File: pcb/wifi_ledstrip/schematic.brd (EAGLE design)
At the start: 160 x 100 mm, 1 part, among them IC1 STM32F10XCXT6

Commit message: main parts added
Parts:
- added HEARTBEAT, LED7, LED8, L_12V, L_3V3, L_5V, L_RX, L_TX: (no value), led:SML1206
- added LED_STRIP_12V, LED_STRIP_GND, LED_STRIP_SIGNAL: (no value), SparkFun-Connectors:SCREWTERMINAL-3.5MM-3
- added POWER: (no value), SparkFun-Connectors:SCREWTERMINAL-5MM-2
- added PROGRAMMER: (no value), SparkFun-Connectors:MOLEX-1X3
- added SW_3, SW_4, SW_RESET, WIFI_RECONNECT: TACTILE_SWITCH_SIDETACTILE_SWITCH_SIDE, mylibrary:TACTILE_SWITCH_SIDE
- added U$1, U$2, U$3: SN74LV1T34, mylibrary:SOT-23-5
- added WIFI_MODUL: ESP01, esp8266modules:ESP01
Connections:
- new net GND: U$1.3, U$2.3, U$3.3
- new net LED_STRIP_SIGNAL_1: U$3.2
- new net LED_STRIP_SIGNAL_2: U$1.2
- new net LED_STRIP_SIGNAL_3: U$2.2
- new net N$1: LED_STRIP_SIGNAL.3, U$2.4
- new net N$2: LED_STRIP_SIGNAL.2, U$1.4
- new net N$3: LED_STRIP_SIGNAL.1, U$3.4
- new net VCC: U$1.5, U$2.5, U$3.5

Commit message: mikrocontroller capacitances, boot pins, reset button added
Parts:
- added C1, C3, C7: (no value), rcl:C1206
- added C10: 1u, rcl:C1206
- added C2: 0.1u, rcl:C1206
- added C4, C5, C6: 100n, rcl:C1206
- added C9: 10n, rcl:C1206
- added C_VDD3: 4.7u, rcl:C1206
- added Q1: 8MHz, special:QS
- added R1, R2, R3, R4, R5, R7, R8, R9: (no value), rcl:R1206
- added R10: 100k, rcl:R1206
- added R11, R6: 10k, rcl:R1206
- HEARTBEAT, LED7, LED8, L_12V, L_3V3, L_5V, L_RX, L_TX: value (none) -> GREEN; device led:SML1206 -> SparkFun-LED:LED-1206
- moved LED_STRIP_SIGNAL 117.7 mm to (-35.6, -119.4)
- moved L_12V 113.5 mm to (3.81, 2.54)
- moved U$3 26.9 mm to (-40.6, -124.5)
- moved U$1 21.7 mm to (-36.8, -129.5), turned to 90 degrees
- moved U$2 18.0 mm to (-31.8, -133.3)
- moved LED_STRIP_12V 4.02 mm to (-8.89, -10.2)
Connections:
- removed net VBAT: IC1.1
- removed net VDDA: IC1.9
- removed net VDD_1: IC1.24
- removed net VDD_2: IC1.36
- removed net VDD_3: IC1.48
- removed net VSSA: IC1.8
- removed net VSS_1: IC1.23
- removed net VSS_2: IC1.35
- removed net VSS_3: IC1.47
- new net BTN_3: SW_3.P$5
- new net BTN_4: SW_4.P$5
- new net BTN_WIFI_RECONNECT: WIFI_RECONNECT.P$5
- new net HEARTBEAT: R7.1
- new net LED7: R8.1
- new net LED8: R9.1
- new net N$10: HEARTBEAT.A, R7.2
- new net N$11: LED7.A, R8.2
- new net N$12: LED8.A, R9.2
- new net N$13: C2.1, IC1.7, SW_RESET.P$3
- new net N$14: C3.1, IC1.5, Q1.2
- new net N$15: C7.1, IC1.6, Q1.1
- new net N$16: IC1.44, R11.2
- new net N$17: PROGRAMMER.2
- new net N$18: PROGRAMMER.3, R10.1
- new net N$4: L_12V.A, R1.1
- new net N$5: L_5V.A, R2.1
- new net N$6: L_3V3.A, R3.1
- new net N$7: L_RX.A, R4.1
- new net N$8: R6.1, WIFI_MODUL.CH_PD
- new net N$9: L_TX.A, R5.1
- new net UART_RX: L_RX.C, WIFI_MODUL.TX
- new net UART_TX: L_TX.C, WIFI_MODUL.RX
- net GND: now also C1.2, C10.2, C2.2, C3.2, C4.2, C5.2, C6.2, C7.2, C9.2, C_VDD3.2, HEARTBEAT.C, IC1.23, IC1.35, IC1.47, IC1.8, LED7.C, LED8.C, LED_STRIP_GND.1, LED_STRIP_GND.2, LED_STRIP_GND.3, L_12V.C, L_3V3.C, L_5V.C, POWER.1, PROGRAMMER.1, R11.1, SW_3.P$3, SW_4.P$3, SW_RESET.P$5, WIFI_MODUL.GND, WIFI_RECONNECT.P$3
- net VCC: now also C1.1, C10.1, C4.1, C5.1, C6.1, C9.1, C_VDD3.1, IC1.1, IC1.24, IC1.36, IC1.48, IC1.9, LED_STRIP_12V.1, LED_STRIP_12V.2, LED_STRIP_12V.3, POWER.2, R1.2, R10.2, R2.2, R3.2, R4.2, R5.2, R6.2, WIFI_MODUL.VCC
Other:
- board size 160 x 100 mm -> 99 x 100 mm

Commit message: parts added, psu symbols fixed
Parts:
- added C11, C15: 8.2n, rcl:C1206
- added C12, C16: 100n, rcl:C1206
- added C13, C14, C17, C8: 22u, rcl:C1206
- added R12, R15: 100k, rcl:R1206
- added R13: 33.2, rcl:R1206
- added R14, R17, R18, R19: 10k, rcl:R1206
- added R16: 56.2k, rcl:R1206
- added SRN4026-4R7M: 4.7u, mylibrary:SRN4026-4R7M
- added TYS60203R3N-10: 3.3u, mylibrary:TYS60203R3N-10
- added U$4, U$5: TPS562219A, mylibrary:SOT23-8L
- C3, C7: value (none) -> 20p
- moved R11 306.7 mm to (45.7, 14.0)
- moved C10 306.7 mm to (45.7, 45.7)
- moved C3 306.7 mm to (45.7, 24.1)
- moved C7 306.7 mm to (45.7, 19.1)
- moved C9 306.7 mm to (45.7, 50.8)
- moved Q1 306.7 mm to (49.5, 31.8)
- moved R10 306.7 mm to (45.7, 7.62)
- moved C1 265.2 mm to (36.8, 66.0)
- moved C2 265.2 mm to (36.8, 45.7)
- moved C4 265.2 mm to (36.8, 35.6)
- moved C5 265.2 mm to (36.8, 30.5)
- moved C6 265.2 mm to (36.8, 25.4)
- moved C_VDD3 265.2 mm to (36.8, 40.6)
- moved R1 265.2 mm to (36.8, 96.5)
- moved R2 265.2 mm to (36.8, 91.4)
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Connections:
- removed net LED7: R8.1
- removed net LED8: R9.1
- removed net VCC: C1.1, C10.1, C4.1, C5.1, C6.1, C9.1, C_VDD3.1, IC1.1, IC1.24, IC1.36, IC1.48, IC1.9, LED_STRIP_12V.1, LED_STRIP_12V.2, LED_STRIP_12V.3, POWER.2, R1.2, R10.2, R2.2, R3.2, R4.2, R5.2, R6.2, U$1.5, U$2.5, U$3.5, WIFI_MODUL.VCC
- new net +12V: C14.1, C8.1, LED_STRIP_12V.1, LED_STRIP_12V.2, LED_STRIP_12V.3, POWER.2, R1.2, R18.1, R19.1, U$4.3, U$5.3
- new net +3V3: C1.1, C10.1, C13.1, C4.1, C5.1, C6.1, C9.1, C_VDD3.1, IC1.1, IC1.24, IC1.36, IC1.48, IC1.9, R10.2, R12.2, R13.2, R3.2, R4.2, R5.2, R6.2, TYS60203R3N-10.P$2, WIFI_MODUL.VCC
- new net +5V: C17.1, R15.2, R16.2, R2.2, SRN4026-4R7M.P$3, U$1.5, U$2.5, U$3.5
- new net LED_7: IC1.3, R8.1
- new net LED_8: IC1.4, R9.1
- new net N$19: IC1.40
- new net N$20: IC1.41
- new net N$21: IC1.42
- new net N$22: IC1.43
- new net N$23: IC1.45
- new net N$24: IC1.46
- new net N$25: C11.1, U$4.5
- new net N$26: C12.1, TYS60203R3N-10.P$1, U$4.2
- new net N$27: IC1.28
- new net N$28: R12.1, U$4.4
- new net N$29: U$4.6
- new net N$30: C15.1, U$5.5
- new net N$31: C16.2, U$5.8
- new net N$32: R13.1, R14.2
- new net N$33: C16.1, SRN4026-4R7M.P$2, U$5.2
- new net N$34: R15.1, U$5.4
- new net N$35: U$5.6
- new net N$36: R16.1, R17.2
- new net N$37: R18.2, U$4.7
- new net N$38: R19.2, U$5.7
- new net SWCLK: IC1.37, PROGRAMMER.2
- new net SWDIO: IC1.34, PROGRAMMER.3, R10.1
- net BTN_3: now also IC1.26
- net BTN_4: now also IC1.27
- net BTN_WIFI_RECONNECT: now also IC1.25
- net GND: now also C11.2, C13.2, C14.2, C15.2, C17.2, C8.2, R14.1, R17.1, U$4.1, U$5.1
- net HEARTBEAT: now also IC1.2
- net LED_STRIP_SIGNAL_1: now also IC1.17
- net LED_STRIP_SIGNAL_2: now also IC1.18
- net LED_STRIP_SIGNAL_3: now also IC1.19
- net N$17: now also C12.2, U$4.8; no longer PROGRAMMER.2
- net N$18: now also IC1.39; no longer PROGRAMMER.3, R10.1
- net UART_RX: now also IC1.31
- net UART_TX: now also IC1.30

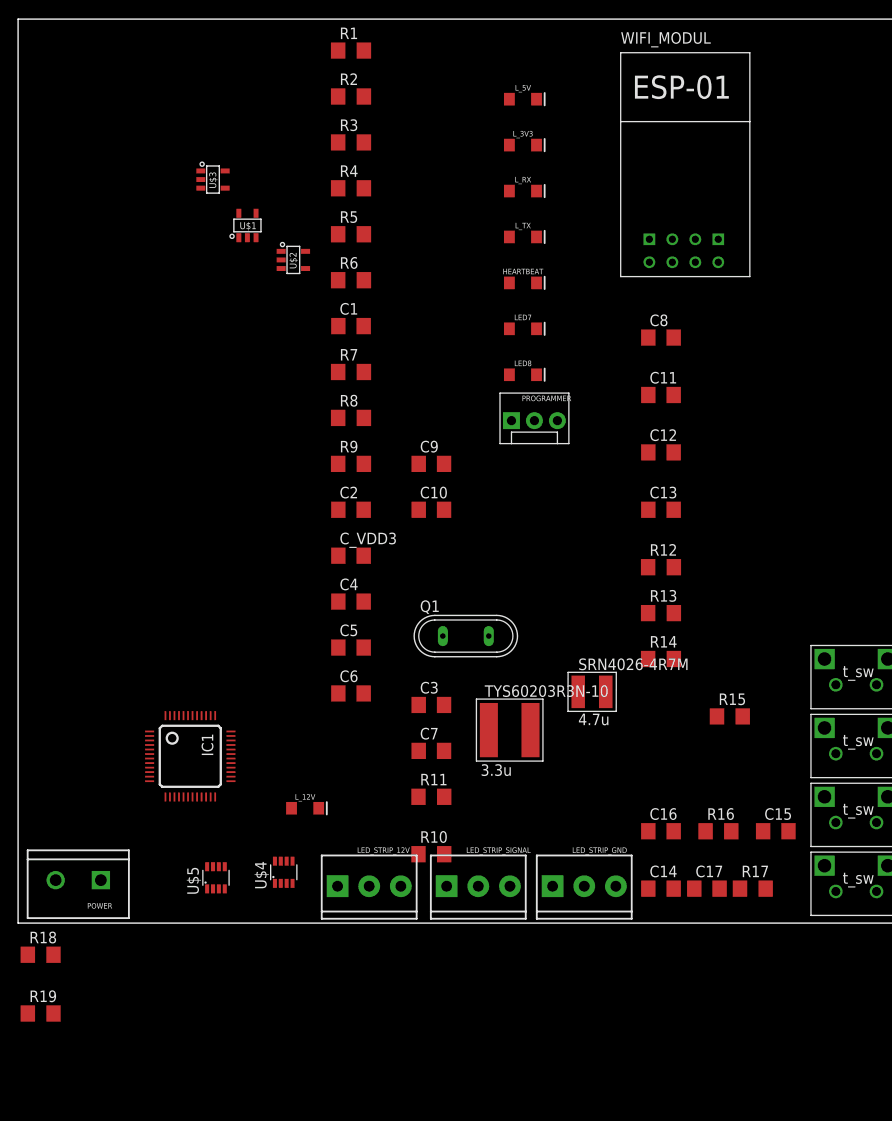
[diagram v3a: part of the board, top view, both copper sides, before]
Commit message: psu 5v half ready
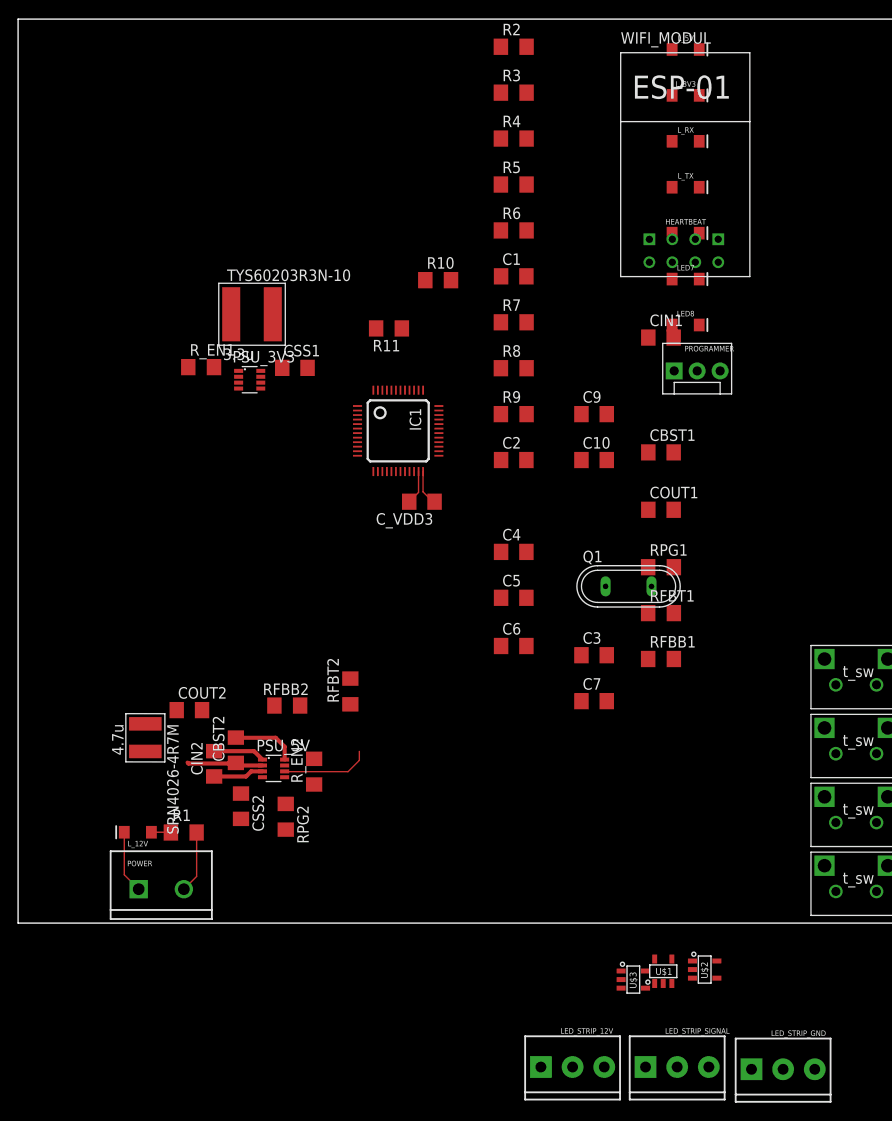
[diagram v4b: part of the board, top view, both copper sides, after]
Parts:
- removed C11, C15: 8.2n, rcl:C1206
- removed C14, C17: 22u, rcl:C1206
- removed C16: 100n, rcl:C1206
- removed R15: 100k, rcl:R1206
- removed R16: 56.2k, rcl:R1206
- removed R17, R18, R19: 10k, rcl:R1206
- removed U$4, U$5: TPS562219A, mylibrary:SOT23-8L
- added CBST2: 100n, rcl:C1206
- added CIN2, COUT2: 22u, rcl:C1206
- added CSS1, CSS2: 8.2n, rcl:C1206
- added PSU_3V3, PSU_5V: TPS562219A, mylibrary:SOT23-8L
- added RFBB2, R_EN1, R_EN2: 10k, rcl:R1206
- added RFBT2: 56.2k, rcl:R1206
- added RPG2: 100k, rcl:R1206
- moved U$3 100.0 mm to (68.1, -6.25)
- moved U$1 94.5 mm to (71.4, -5.33)
- moved U$2 90.7 mm to (76.0, -5.14)
- moved R1 88.5 mm to (18.3, 10.0)
- moved R10 63.5 mm to (46.5, 71.1)
- moved TYS60203R3N-10 54.1 mm to (25.9, 67.3)
- moved R11 52.0 mm to (41.0, 65.8), turned to 180 degrees
- moved SRN4026-4R7M 48.0 mm to (14.1, 22.0), turned to 270 degrees
- moved IC1 42.7 mm to (42.0, 54.5)
- moved LED_STRIP_12V 30.1 mm to (57.8, -15.9)
- moved LED_STRIP_GND 29.9 mm to (81.1, -16.2)
- moved LED_STRIP_SIGNAL 29.7 mm to (69.4, -15.9)
- moved C1 18.8 mm to (54.8, 71.5)
- moved C10 18.8 mm to (63.7, 51.2)
- moved C2 18.8 mm to (54.8, 51.2)
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- renumbered C12 to CBST1, C13 to COUT1, C8 to CIN1, R12 to RPG1, R13 to RFBT1, R14 to RFBB1
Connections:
- removed net N$29: U$4.6
- removed net N$36: R16.1, R17.2
- net +12V: now also CIN2.1, PSU_3V3.3, PSU_5V.3, R_EN1.1, R_EN2.1; no longer C14.1, R18.1, R19.1, U$4.3, U$5.3
- net +5V: now also COUT2.1, RFBT2.2, RPG2.2; no longer C17.1, R15.2, R16.2
- net GND: now also CIN2.2, COUT2.2, CSS1.2, CSS2.2, PSU_3V3.1, PSU_5V.1, RFBB2.1; no longer C11.2, C14.2, C15.2, C17.2, R17.1, U$4.1, U$5.1
- net N$17: now also PSU_3V3.8; no longer U$4.8
- net N$25: now also CSS1.1, PSU_3V3.4; no longer C11.1, U$4.5
- net N$26: now also PSU_3V3.2; no longer U$4.2
- net N$28: now also PSU_3V3.5; no longer U$4.4
- net N$30: now also CSS2.1, PSU_5V.4; no longer C15.1, U$5.5
- net N$31: now also CBST2.2, PSU_5V.8; no longer C16.2, U$5.8
- net N$32: now also PSU_3V3.6
- net N$33: now also CBST2.1, PSU_5V.2; no longer C16.1, U$5.2
- net N$34: now also PSU_5V.5, RPG2.1; no longer R15.1, U$5.4
- net N$35: now also PSU_5V.6, RFBB2.2, RFBT2.1; no longer U$5.6
- net N$37: now also PSU_3V3.7, R_EN1.2; no longer R18.2, U$4.7
- net N$38: now also PSU_5V.7, R_EN2.2; no longer R19.2, U$5.7
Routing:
- net GND: track 0.00 -> 16.5 mm
- net +12V: track 0.00 -> 12.4 mm
- net N$35: track 0.00 -> 9.80 mm
- net N$33: track 0.00 -> 8.47 mm
- net N$31: track 0.00 -> 7.24 mm
- net +3V3: track 0.00 -> 3.97 mm
- net N$4: track 0.00 -> 2.17 mm

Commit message: psu 5v and 3v3 ready
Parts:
- moved CIN1 61.8 mm to (16.2, 36.4), turned to 90 degrees
- moved COUT1 59.1 mm to (12.1, 42.0)
- moved CBST1 54.3 mm to (18.7, 37.9), turned to 90 degrees
- moved RFBB1 50.6 mm to (22.1, 42.0)
- moved RFBT1 43.3 mm to (28.7, 42.9), turned to 90 degrees
- moved RPG1 40.4 mm to (30.9, 42.9), turned to 90 degrees
- moved Q1 38.0 mm to (34.2, 55.5), turned to 90 degrees
- moved TYS60203R3N-10 34.9 mm to (8.40, 37.1), turned to 90 degrees
- moved CSS1 31.5 mm to (19.7, 31.9), turned to 270 degrees
- moved R_EN1 26.9 mm to (25.9, 35.2), turned to 90 degrees
- moved PSU_3V3 24.4 mm to (22.6, 35.9)
- moved RPG2 17.9 mm to (43.2, 23.4), turned to 90 degrees
- moved WIFI_MODUL 15.8 mm to (89.4, 82.0)
- moved CSS2 8.50 mm to (33.2, 13.2)
- moved CBST2 7.25 mm to (31.3, 19.1)
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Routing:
- net GND: track 16.5 -> 71.0 mm
- net +12V: track 12.4 -> 57.3 mm
- net +5V: track 0.00 -> 31.7 mm
- net +3V3: track 3.97 -> 33.9 mm
- net N$32: track 0.00 -> 15.4 mm
- net N$26: track 0.00 -> 13.9 mm
- net N$28: track 0.00 -> 11.8 mm
- net N$34: track 0.00 -> 10.6 mm
- net N$33: track 8.47 -> 16.3 mm
- net N$17: track 0.00 -> 7.08 mm
- net N$35: track 9.80 -> 13.6 mm
- net N$25: track 0.00 -> 2.62 mm
- net N$30: track 0.00 -> 2.26 mm
- net N$37: track 0.00 -> 2.26 mm
- net N$38: track 0.00 -> 2.22 mm
- added copper zone on layer 1, net GND

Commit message: psu fixed
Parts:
- moved L_5V 112.2 mm to (5.70, 7.52), turned to 270 degrees
- moved L_3V3 109.8 mm to (3.14, 7.52), turned to 270 degrees
- moved R2 97.5 mm to (5.84, 12.6), turned to 90 degrees
- moved R3 94.6 mm to (3.17, 12.6), turned to 90 degrees
- moved C1 72.9 mm to (-16.4, 87.0)
- moved C10 72.9 mm to (-7.53, 66.7)
- moved C2 72.9 mm to (-16.4, 66.7)
- moved C3 72.9 mm to (-7.53, 45.1)
- moved C4 72.9 mm to (-16.4, 56.6)
- moved C5 72.9 mm to (-16.4, 51.5)
- moved C6 72.9 mm to (-16.4, 46.1)
- moved C7 72.9 mm to (-7.53, 40.0)
- moved C9 72.9 mm to (-7.53, 71.8)
- moved R4 72.9 mm to (-16.4, 102.3)
- moved R5 72.9 mm to (-16.4, 97.2)
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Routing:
- net +5V: track 31.7 -> 121.5 mm, vias 0 -> 8
- net +12V: track 57.3 -> 81.1 mm, vias 0 -> 13
- net +3V3: track 33.9 -> 48.6 mm, vias 0 -> 8
- net GND: track 71.0 -> 82.4 mm, vias 0 -> 23
- net N$3: track 0.00 -> 6.79 mm
- net N$2: track 0.00 -> 6.78 mm
- net N$1: track 0.00 -> 6.77 mm
- net N$33: track 16.3 -> 10.2 mm
- net N$5: track 0.00 -> 2.24 mm
- net N$6: track 0.00 -> 2.19 mm
- net N$32: track 15.4 -> 13.4 mm
- net N$28: track 11.8 -> 11.3 mm
- added copper zone on layer 1, net +12V
- added copper zone on layer 16, net +12V
- added copper zone on layer 1, net +3V3
- added copper zone on layer 1, net +5V
- added copper zone on layer 16, net +5V

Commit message: final size set
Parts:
- moved C1 99.9 mm to (68.8, 34.9), turned to 270 degrees
- moved R6 95.5 mm to (63.6, 40.1), turned to 90 degrees
- moved HEARTBEAT 91.2 mm to (17.6, 47.2), turned to 180 degrees
- moved LED7 91.2 mm to (17.6, 43.3), turned to 180 degrees
- moved LED8 91.2 mm to (17.6, 39.6), turned to 180 degrees
- moved R4 89.5 mm to (38.5, 31.6), flipped to the bottom, turned to 90 degrees
- moved SW_RESET 86.5 mm to (6.71, 38.3), turned to 270 degrees
- moved R5 83.2 mm to (34.7, 31.6), flipped to the bottom, turned to 90 degrees
- moved C4 73.6 mm to (51.2, 27.4), turned to 180 degrees
- moved L_RX 72.5 mm to (43.4, 28.2)
- moved C6 72.0 mm to (55.4, 41.8), turned to 270 degrees
- moved L_TX 71.9 mm to (43.4, 30.6)
- moved C9 63.5 mm to (44.2, 34.9), flipped to the bottom, turned to 90 degrees
- moved C5 61.8 mm to (44.9, 44.3)
- moved C10 53.7 mm to (40.5, 42.7), flipped to the bottom
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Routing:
- net GND: track 82.4 -> 272.4 mm, vias 23 -> 51
- net +3V3: track 48.6 -> 149.8 mm, vias 8 -> 12
- net N$13: track 0.00 -> 50.4 mm, vias 0 -> 2
- net LED_STRIP_SIGNAL_3: track 0.00 -> 24.9 mm, vias 0 -> 2
- net SWCLK: track 0.00 -> 23.9 mm
- net LED_STRIP_SIGNAL_2: track 0.00 -> 23.7 mm, vias 0 -> 2
- net LED_STRIP_SIGNAL_1: track 0.00 -> 22.9 mm, vias 0 -> 2
- net HEARTBEAT: track 0.00 -> 22.4 mm
- net SWDIO: track 0.00 -> 21.2 mm
- net LED_7: track 0.00 -> 20.9 mm
- net LED_8: track 0.00 -> 19.6 mm
- net N$15: track 0.00 -> 8.03 mm, vias 0 -> 1
- net N$14: track 0.00 -> 7.84 mm, vias 0 -> 1
- net N$16: track 0.00 -> 5.08 mm
- net N$11: track 0.00 -> 2.89 mm
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- added copper zone on layer 16, net +3V3
- added copper zone on layer 16, net GND
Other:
- board size 99 x 100 mm -> 80 x 49.5 mm

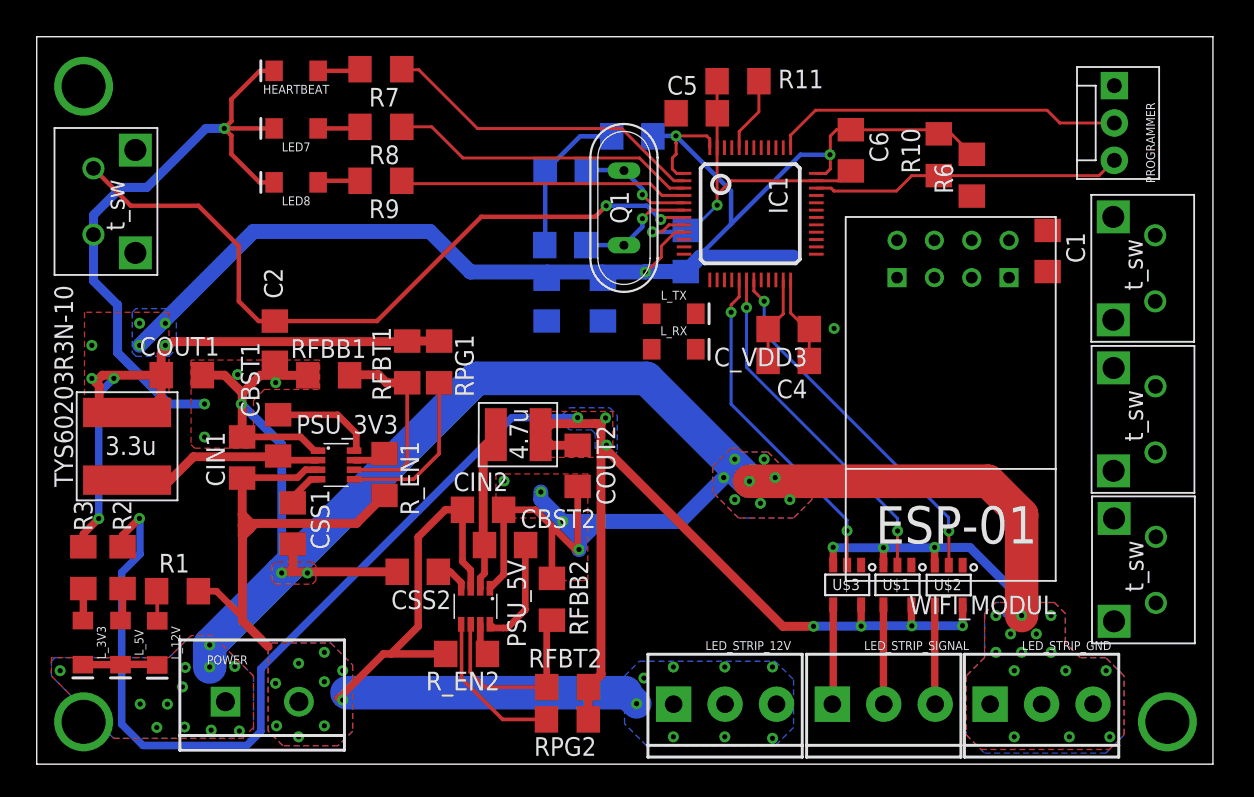
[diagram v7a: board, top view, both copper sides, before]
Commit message: beta pcb - resistor values need to be calculated
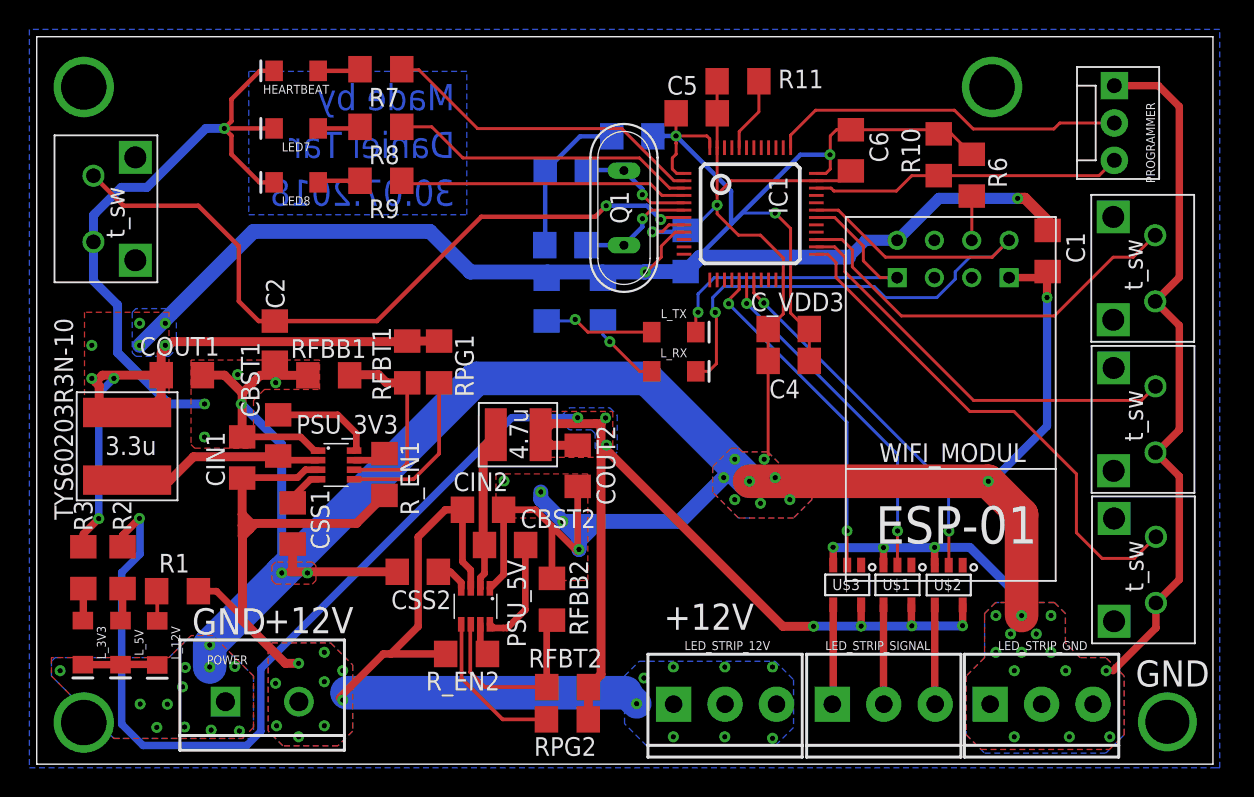
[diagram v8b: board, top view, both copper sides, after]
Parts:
- moved L_RX 1.50 mm to (43.4, 26.7)
- moved L_TX 1.25 mm to (43.4, 29.4)
- moved SW_RESET 0.50 mm to (6.71, 37.8)
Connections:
- removed net N$18: IC1.39
- removed net N$19: IC1.40
- removed net N$20: IC1.41
- removed net N$21: IC1.42
- removed net N$22: IC1.43
- removed net N$23: IC1.45
- removed net N$24: IC1.46
- removed net N$27: IC1.28
- net BTN_4: now also IC1.25; no longer IC1.27
- net BTN_WIFI_RECONNECT: now also IC1.27; no longer IC1.25
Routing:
- net GND: track 272.4 -> 350.7 mm, vias 51 -> 53
- net UART_RX: track 0.00 -> 43.8 mm, vias 0 -> 1
- net BTN_4: track 0.00 -> 35.2 mm
- net +3V3: track 149.8 -> 179.6 mm, vias 12 -> 13
- net BTN_3: track 0.00 -> 28.4 mm
- net BTN_WIFI_RECONNECT: track 0.00 -> 28.2 mm
- net UART_TX: track 0.00 -> 24.4 mm, vias 0 -> 1
- net N$9: track 0.00 -> 7.55 mm, vias 0 -> 1
- net N$7: track 0.00 -> 5.29 mm, vias 0 -> 1
- net N$8: track 0.00 -> 3.01 mm
- net +12V: track 81.4 -> 83.3 mm
- net N$33: track 10.2 -> 11.0 mm
- added copper zone on layer 16, net SIGNATURE
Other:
- board text added: "+12V"
- board text added: "30.07.2018"
- board text added: "Daniel Tar"
- board text added: "GND"
- board text added: "Made by"
